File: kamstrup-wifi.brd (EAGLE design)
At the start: 36 x 89.3 mm, 26 parts, among them T1 BT137, T2 BT137, U1 ESP8266-07, U2 MCP1316T-29LE/OT

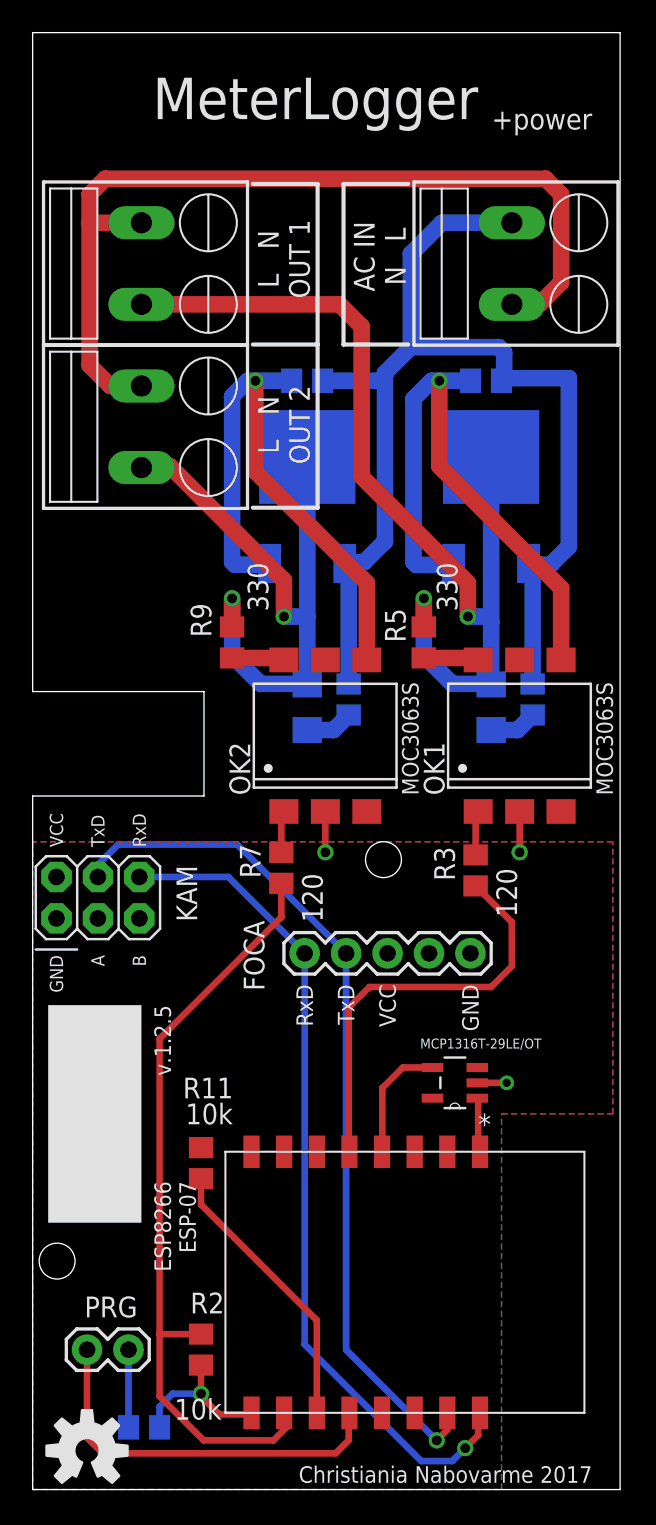
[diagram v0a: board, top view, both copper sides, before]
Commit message: rotated jp1, jp3 and jp3
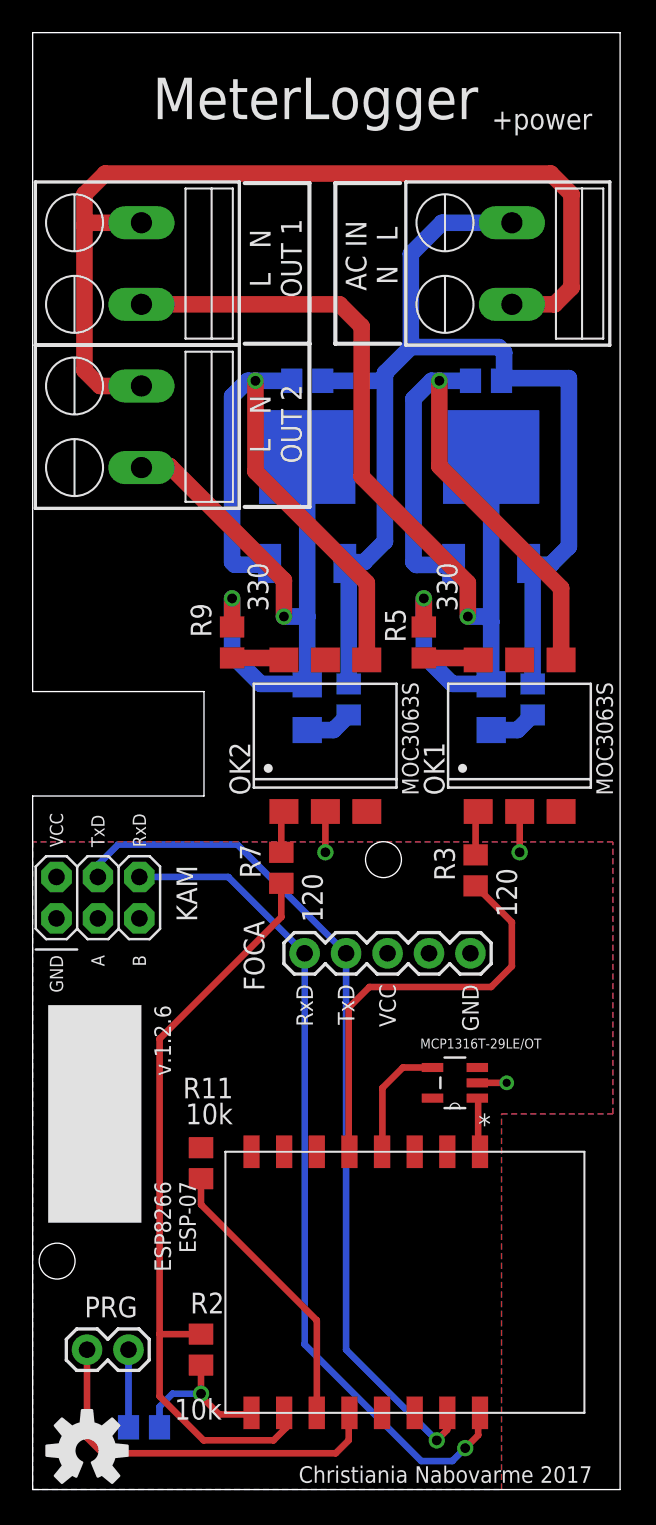
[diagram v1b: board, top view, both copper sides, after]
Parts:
- moved JP1 5.00 mm to (29.4, 72.6), turned to 90 degrees
- moved JP2 5.00 mm to (6.67, 72.6), turned to 90 degrees
- moved JP3 5.00 mm to (6.67, 62.6), turned to 90 degrees
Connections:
- net N$15: now also JP2.1; no longer JP2.2
- net N$18: now also JP1.1, JP2.2, JP3.2; no longer JP1.2, JP2.1, JP3.1
- net N$8: now also JP3.1; no longer JP3.2
- net N$9: now also JP1.2; no longer JP1.1
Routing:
- net N$18: track 56.0 -> 58.9 mm
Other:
- board text added: "v.1.2.6"
- board text removed: "v.1.2.5"
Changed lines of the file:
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@@
 <setting verticaltext="up"/>
 </settings>
-<grid distance="0.025" unitdist="inch" unit="mm" style="lines" multiple="1" display="no" altdistance="0.0025" altunitdist="inch" altunit="mm"/>
+<grid distance="0.05" unitdist="mm" unit="mm" style="lines" multiple="1" display="no" altdistance="0.005" altunitdist="mm" altunit="mm"/>
 <layers>
 <layer number="1" name="Top" color="4" fill="1" visible="yes" active="yes"/>
@@
 <text x="7.46125" y="18.89125" size="1.016" layer="25" ratio="10" rot="R270">ESP8266
 ESP-07</text>
-<text x="7.46125" y="29.68625" size="1.016" layer="25" ratio="15" rot="R270">v.1.2.5</text>
+<text x="7.46125" y="29.68625" size="1.016" layer="25" ratio="15" rot="R270">v.1.2.6</text>
 <text x="26.82875" y="30.95625" size="1.016" layer="25" rot="R90" align="center-right">GND</text>
-<text x="21.2725" y="75.565" size="1.27" layer="25" ratio="20" rot="R90" align="center">AC IN
+<text x="20.7725" y="75.615" size="1.27" layer="25" ratio="20" rot="R90" align="center">AC IN
 N   L</text>
 <text x="27.6225" y="13.0175" size="1.016" layer="26" font="fixed" rot="MR0">Part            RS#
@@
 <wire x1="28.41625" y1="13.81125" x2="28.41625" y2="29.845" width="0.1524" layer="26"/>
 <wire x1="14.2875" y1="29.845" x2="14.2875" y2="13.81125" width="0.1524" layer="26"/>
-<wire x1="13.49375" y1="80.01" x2="17.4625" y2="80.01" width="0.254" layer="25"/>
-<wire x1="17.4625" y1="80.01" x2="17.4625" y2="70.1675" width="0.254" layer="25"/>
-<wire x1="17.4625" y1="70.1675" x2="17.4625" y2="60.16625" width="0.254" layer="25"/>
-<wire x1="17.4625" y1="60.16625" x2="13.49375" y2="60.16625" width="0.254" layer="25"/>
-<wire x1="17.4625" y1="70.1675" x2="13.49375" y2="70.1675" width="0.254" layer="25"/>
-<wire x1="19.05" y1="80.01" x2="23.01875" y2="80.01" width="0.254" layer="25"/>
-<wire x1="19.05" y1="70.1675" x2="23.01875" y2="70.1675" width="0.254" layer="25"/>
-<wire x1="19.05" y1="80.01" x2="19.05" y2="70.1675" width="0.254" layer="25"/>
+<wire x1="12.99375" y1="80.06" x2="16.9625" y2="80.06" width="0.254" layer="25"/>
+<wire x1="16.9625" y1="80.06" x2="16.9625" y2="70.2175" width="0.254" layer="25"/>
+<wire x1="16.9625" y1="70.2175" x2="16.9625" y2="60.21625" width="0.254" layer="25"/>
+<wire x1="16.9625" y1="60.21625" x2="12.99375" y2="60.21625" width="0.254" layer="25"/>
+<wire x1="16.9625" y1="70.2175" x2="12.99375" y2="70.2175" width="0.254" layer="25"/>
+<wire x1="18.55" y1="80.06" x2="22.51875" y2="80.06" width="0.254" layer="25"/>
+<wire x1="18.55" y1="70.2175" x2="22.51875" y2="70.2175" width="0.254" layer="25"/>
+<wire x1="18.55" y1="80.06" x2="18.55" y2="70.2175" width="0.254" layer="25"/>
 <text x="27.305" y="83.97875" size="2.54" layer="25" ratio="15" rot="R180" align="top-left">MeterLogger</text>
 <rectangle x1="0.9525" y1="16.35125" x2="6.6675" y2="29.68625" layer="25"/>
-<text x="15.39875" y="75.40625" size="1.27" layer="25" ratio="20" rot="R270" align="center">L   N
+<text x="14.89875" y="75.45625" size="1.27" layer="25" ratio="20" rot="R270" align="center">L   N
 OUT 1</text>
-<text x="15.39875" y="65.24625" size="1.27" layer="25" ratio="20" rot="R270" align="center">L   N
+<text x="14.89875" y="65.29625" size="1.27" layer="25" ratio="20" rot="R270" align="center">L   N
 OUT 2</text>
 <text x="34.29" y="1.42875" size="1.016" layer="25" ratio="15" rot="R180">Christiania Nabovarme 2017</text>
@@
 <attribute name="VALUE" x="16.8275" y="44.7675" size="1.27" layer="26" rot="MR270"/>
 </element>
-<element name="JP3" library="TE Terminal Block 45 degrees" package="SCREWTERMINAL-5MM-2" value="AC OUT 2" x="6.6675" y="67.6275" smashed="yes" rot="R270"/>
+<element name="JP3" library="TE Terminal Block 45 degrees" package="SCREWTERMINAL-5MM-2" value="AC OUT 2" x="6.6675" y="62.6275" smashed="yes" rot="R90"/>
 <element name="OK1" library="optocoupler" package="DIL6-SMD" value="MOC3063S" x="29.845" y="46.19625" smashed="yes">
 <attribute name="MF" value="FAIRCHILD SEMICONDUCTOR" x="23.01875" y="46.19625" size="1.778" layer="27" display="off"/>
@@
 <attribute name="VALUE" x="28.41625" y="44.92625" size="1.27" layer="26" rot="MR270"/>
 </element>
-<element name="JP1" library="TE Terminal Block 45 degrees" package="SCREWTERMINAL-5MM-2" value="AC IN" x="29.36875" y="77.62875" smashed="yes" rot="R270"/>
-<element name="JP2" library="TE Terminal Block 45 degrees" package="SCREWTERMINAL-5MM-2" value="AC OUT 1" x="6.6675" y="77.62875" smashed="yes" rot="R270"/>
+<element name="JP1" library="TE Terminal Block 45 degrees" package="SCREWTERMINAL-5MM-2" value="AC IN" x="29.36875" y="72.62875" smashed="yes" rot="R90"/>
+<element name="JP2" library="TE Terminal Block 45 degrees" package="SCREWTERMINAL-5MM-2" value="AC OUT 1" x="6.6675" y="72.62875" smashed="yes" rot="R90"/>
 <element name="T1" library="Triac SOT428" package="SOT428" value="BT137" x="28.09875" y="59.84875" smashed="yes" rot="MR0">
 <attribute name="NAME" x="24.3205" y="65.30975" size="1.27" layer="26" rot="MR0"/>
@@
 <wire x1="13.97" y1="49.37125" x2="16.79875" y2="49.37125" width="1.016" layer="16"/>
 <wire x1="16.79875" y1="49.37125" x2="16.8275" y2="49.3425" width="1.016" layer="16"/>
-<contactref element="JP3" pad="2"/>
-<wire x1="6.6675" y1="62.6275" x2="8.335" y2="62.6275" width="1.016" layer="1"/>
 <wire x1="8.335" y1="62.6275" x2="8.41375" y2="62.70625" width="1.016" layer="1"/>
+<contactref element="JP3" pad="1"/>
+<wire x1="6.6675" y1="62.6275" x2="6.74625" y2="62.70625" width="1.016" layer="1"/>
+<wire x1="6.74625" y1="62.70625" x2="8.41375" y2="62.70625" width="1.016" layer="1"/>
 <wire x1="16.8275" y1="63.02375" x2="16.8275" y2="63.27495" width="0" layer="19" extent="16-16"/>
 </signal>
@@
 <contactref element="R4" pad="2"/>
 <contactref element="R6" pad="1"/>
-<contactref element="JP1" pad="1"/>
 <wire x1="19.3675" y1="49.36875" x2="19.3675" y2="56.52135" width="1.016" layer="16"/>
 <wire x1="30.63875" y1="49.36875" x2="30.63875" y2="56.52135" width="1.016" layer="16"/>
@@
 <wire x1="21.2725" y1="67.945" x2="21.59" y2="68.2625" width="1.016" layer="16"/>
 <wire x1="28.8925" y1="68.10625" x2="32.86125" y2="68.10625" width="1.016" layer="16"/>
-<wire x1="29.36875" y1="77.62875" x2="25.0825" y2="77.62875" width="1.016" layer="16"/>
 <wire x1="25.0825" y1="77.62875" x2="23.1775" y2="75.72375" width="1.016" layer="16"/>
 <wire x1="23.1775" y1="75.72375" x2="23.1775" y2="70.00875" width="1.016" layer="16"/>
+<contactref element="JP1" pad="2"/>
+<wire x1="29.36875" y1="77.62875" x2="25.0825" y2="77.62875" width="1.016" layer="16"/>
 <wire x1="30.48635" y1="56.67375" x2="30.39875" y2="56.74995" width="0" layer="19" extent="16-16"/>
 <wire x1="19.1275" y1="56.74995" x2="19.22145" y2="56.8325" width="0" layer="19" extent="16-16"/>
@@
 <wire x1="25.7175" y1="49.37125" x2="28.07" y2="49.37125" width="1.016" layer="16"/>
 <wire x1="28.07" y1="49.37125" x2="28.09875" y2="49.3425" width="1.016" layer="16"/>
-<contactref element="JP2" pad="2"/>
-<wire x1="6.6675" y1="72.62875" x2="18.81125" y2="72.62875" width="1.016" layer="1"/>
-<wire x1="18.81125" y1="72.62875" x2="20.16125" y2="71.27875" width="1.016" layer="1"/>
+<wire x1="20.16125" y1="71.27875" x2="18.81125" y2="72.62875" width="1.016" layer="1"/>
+<contactref element="JP2" pad="1"/>
+<wire x1="18.81125" y1="72.62875" x2="6.6675" y2="72.62875" width="1.016" layer="1"/>
 </signal>
 <signal name="N$17">
@@
 <wire x1="28.09875" y1="46.5425" x2="29.7125" y2="46.5425" width="1.016" layer="16"/>
 <wire x1="29.7125" y1="46.5425" x2="30.63875" y2="47.46875" width="1.016" layer="16"/>
-</signal>
-<signal name="N$18">
-<contactref element="JP1" pad="2"/>
-<wire x1="29.36875" y1="72.62875" x2="31.03625" y2="72.62875" width="1.016" layer="1"/>
-<wire x1="31.03625" y1="72.62875" x2="32.385" y2="73.9775" width="1.016" layer="1"/>
-<wire x1="32.385" y1="73.9775" x2="32.385" y2="79.375" width="1.016" layer="1"/>
-<wire x1="32.385" y1="79.375" x2="31.4325" y2="80.3275" width="1.016" layer="1"/>
-<wire x1="31.4325" y1="80.3275" x2="4.445" y2="80.3275" width="1.016" layer="1"/>
-<wire x1="4.445" y1="80.3275" x2="3.4925" y2="79.375" width="1.016" layer="1"/>
-<wire x1="3.4925" y1="77.62875" x2="3.4925" y2="79.375" width="1.016" layer="1"/>
-<wire x1="3.4925" y1="77.62875" x2="3.4925" y2="68.8975" width="1.016" layer="1"/>
-<wire x1="4.7625" y1="67.6275" x2="3.4925" y2="68.8975" width="1.016" layer="1"/>
-<contactref element="JP2" pad="1"/>
-<contactref element="JP3" pad="1"/>
-<wire x1="6.6675" y1="77.62875" x2="3.4925" y2="77.62875" width="1.016" layer="1"/>
-<wire x1="6.6675" y1="67.6275" x2="4.7625" y2="67.6275" width="1.016" layer="1"/>
 </signal>
 <signal name="N$11">
@@
 <wire x1="10.31875" y1="17.4625" x2="10.31875" y2="19.0525" width="0.4064" layer="1"/>
 </signal>
+<signal name="N$18">
+<contactref element="JP3" pad="2"/>
+<contactref element="JP1" pad="1"/>
+<contactref element="JP2" pad="2"/>
+<wire x1="29.36875" y1="72.62875" x2="31.98875" y2="72.62875" width="1.016" layer="1"/>
+<wire x1="31.98875" y1="72.62875" x2="33.02" y2="73.66" width="1.016" layer="1"/>
+<wire x1="33.02" y1="73.66" x2="33.02" y2="79.375" width="1.016" layer="1"/>
+<wire x1="33.02" y1="79.375" x2="31.75" y2="80.645" width="1.016" layer="1"/>
+<wire x1="31.75" y1="80.645" x2="4.445" y2="80.645" width="1.016" layer="1"/>
+<wire x1="4.445" y1="80.645" x2="3.175" y2="79.375" width="1.016" layer="1"/>
+<wire x1="3.175" y1="77.47" x2="3.175" y2="79.375" width="1.016" layer="1"/>
+<wire x1="3.175" y1="77.47" x2="3.175" y2="68.58" width="1.016" layer="1"/>
+<wire x1="3.175" y1="68.58" x2="4.1275" y2="67.6275" width="1.016" layer="1"/>
+<wire x1="4.1275" y1="67.6275" x2="6.6675" y2="67.6275" width="1.016" layer="1"/>
+<wire x1="6.6675" y1="77.62875" x2="3.33375" y2="77.62875" width="1.016" layer="1"/>
+<wire x1="3.33375" y1="77.62875" x2="3.175" y2="77.47" width="1.016" layer="1"/>
+</signal>
 </signals>

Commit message: removed snubber circuits and external watchdog timer ic now version 1.3.0
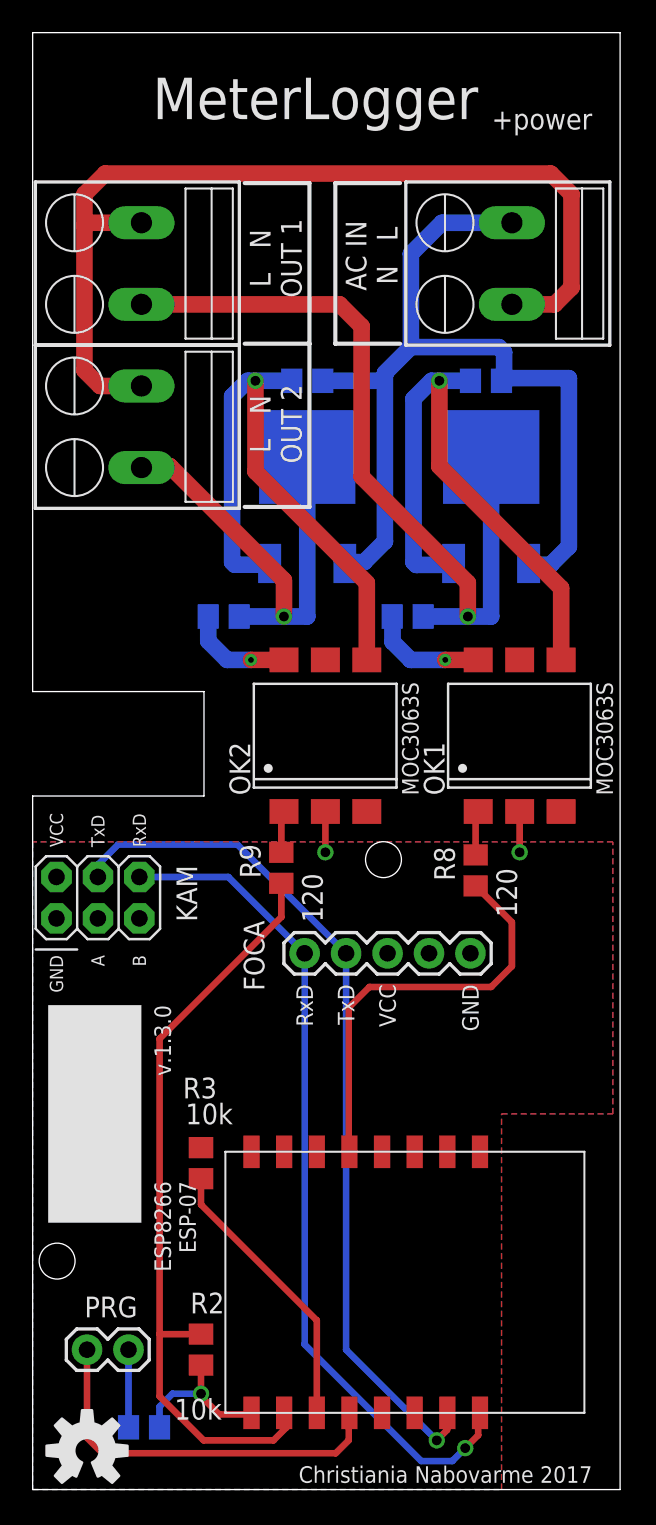
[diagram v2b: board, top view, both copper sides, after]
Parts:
- removed C1, C2: 10nF, rcl:C1206
- removed R10: 39, rcl:R0805
- removed R11: 10k, rcl:R0805
- removed U2: MCP1316T-29LE/OT, Microchip_By_element14_Batch_1:SOT95P270X145-5N
- R3: value 120 -> 10k
- R6: value 39 -> 330
- R7: value 120 -> 330
- R8, R9: value 330 -> 120
- moved R8 31.7 mm to (27.1, 37.9), flipped to the top, turned to 90 degrees
- moved R3 24.6 mm to (10.3, 20.0), turned to 270 degrees
- moved R6 23.9 mm to (16.8, 67.9), turned to 180 degrees
- moved R7 15.8 mm to (11.7, 53.5), flipped to the bottom, turned to 180 degrees
- moved R9 14.1 mm to (15.2, 38.1)
- moved R5 1.87 mm to (23.0, 53.5), flipped to the bottom, turned to 180 degrees
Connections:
- removed net N$10: C2.2, R10.2
- removed net N$17: C1.2, R6.2
- removed net N$19: U1.REST, U2.1
- removed net N$20: U1.GPIO16, U2.4
- net 3.3V: now also R3.1; no longer R11.1, U2.5
- net GND: no longer U2.2
- net N$11: now also R8.1; no longer R3.1
- net N$12: now also R8.2; no longer R3.2
- net N$15: no longer C1.1
- net N$16: now also R9.1; no longer R7.1
- net N$21: now also R3.2; no longer R11.2
- net N$5: now also R9.2; no longer R7.2
- net N$6: now also R6.1; no longer R8.1
- net N$7: now also R7.1; no longer R9.1
- net N$8: now also R7.2; no longer C2.1, R9.2
- net N$9: now also R6.2; no longer R10.1, R6.1, R8.2
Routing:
- net N$9: track 71.2 -> 56.9 mm
- net N$8: track 39.7 -> 27.7 mm, vias 2 -> 1
- net N$15: track 60.1 -> 48.5 mm, vias 2 -> 1
- net N$20: track 7.51 -> 0.00 mm
- net N$14: track 3.38 -> 7.27 mm, vias 0 -> 1
- net N$7: track 3.22 -> 6.62 mm, vias 0 -> 1
- net N$19: track 3.35 -> 0.00 mm
- net N$17: track 2.92 -> 0.00 mm
- net N$10: track 2.92 -> 0.00 mm
- net GND: track 17.8 -> 16.0 mm, vias 4 -> 3
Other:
- board text added: "Part RS# JP1, JP2, JP3 821-8701 KAM 702-2937 OK1, OK2 691-2319 R1, R2, R3 721-7820 R4, R5, R6, R7 721-7707 R8, R9 721-6867 T1, T2 792-0709"
- board text added: "v.1.3.0"
- board text removed: "Part RS# C1, C2 766-1150 JP1, JP2, JP3 821-8701 KAM 702-2937 OK1, OK2 691-2319 R1, R2, R11 721-7820 R3, R7 721-6867 R4, R5, R8, R9 721-7707 R6, R10 770-8798 T1, T2 792-0709"
- board text removed: "v.1.2.6"
